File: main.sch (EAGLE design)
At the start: 7 parts

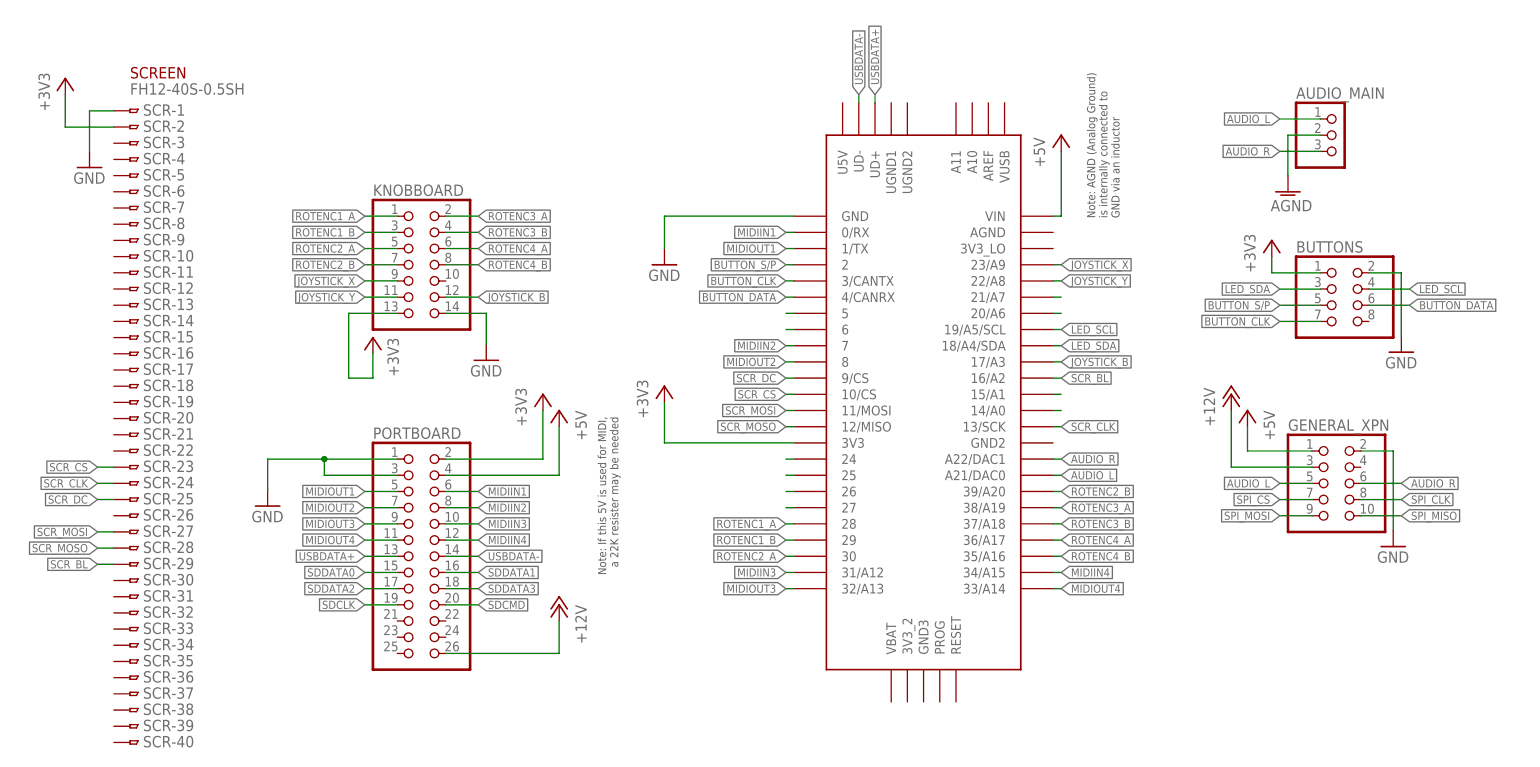
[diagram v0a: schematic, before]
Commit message: xpn-SPI connected, portboard audio added
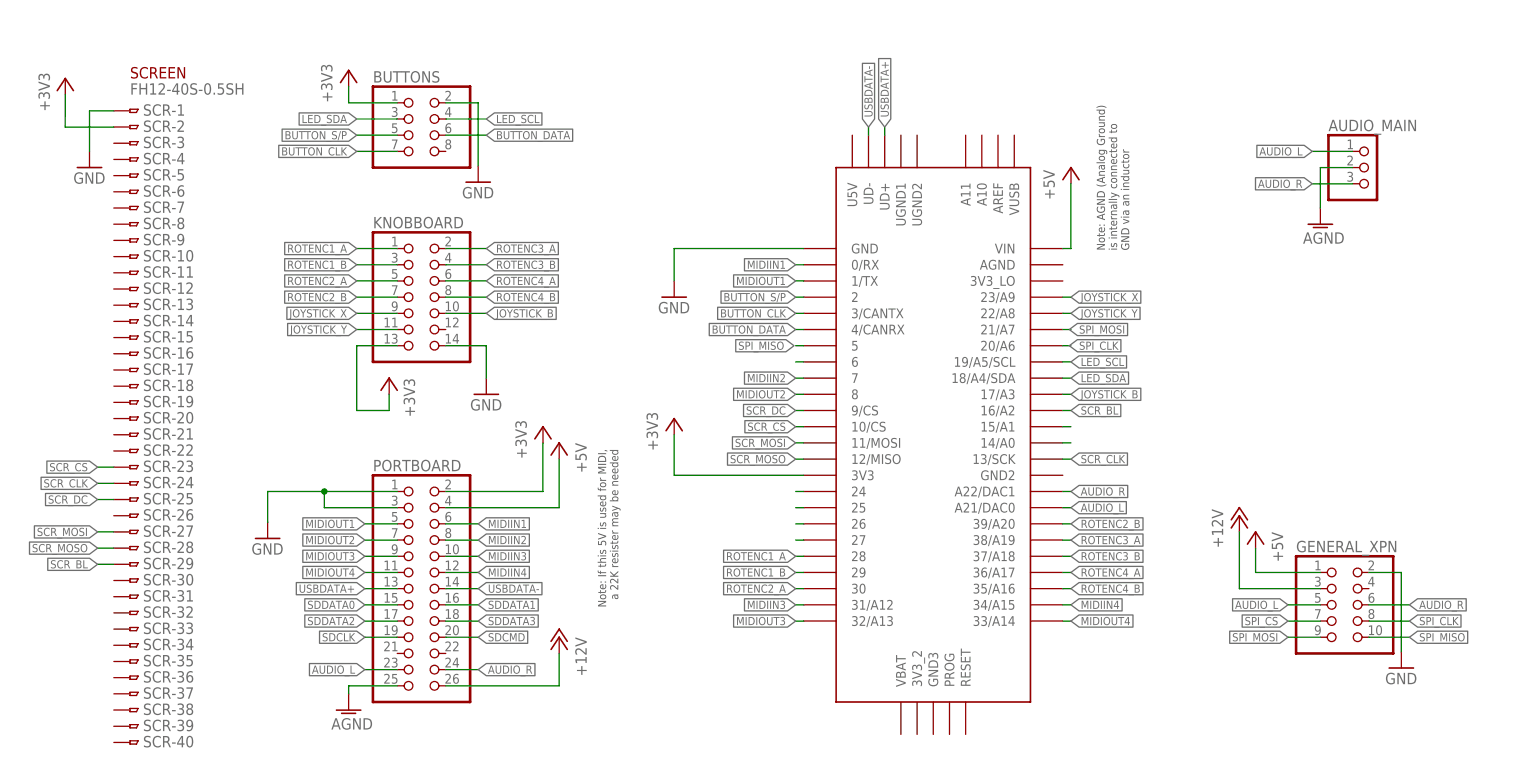
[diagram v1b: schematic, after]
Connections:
- removed net N$1: U$1.5
- removed net N$20: U$1.21/A7
- removed net N$21: U$1.20/A6
- net AGND: now also PORTBOARD.25
- net AUDIO_L: now also PORTBOARD.23
- net AUDIO_R: now also PORTBOARD.24
- net JOYSTICK_B: now also KNOBBOARD.10; no longer KNOBBOARD.12
- net SPI_CLK: now also U$1.20/A6
- net SPI_MISO: now also U$1.5
- net SPI_MOSI: now also U$1.21/A7
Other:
- moved on the sheet: AUDIO_MAIN, BUTTONS, GENERAL_XPN, KNOBBOARD, PORTBOARD

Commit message: milestone, reroute
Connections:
- net AUDIO_L: now also GENERAL_XPN.7; no longer GENERAL_XPN.5
- net AUDIO_R: now also GENERAL_XPN.9; no longer GENERAL_XPN.6
- net GND: now also GENERAL_XPN.5; no longer GENERAL_XPN.2
- net SPI_CLK: now also GENERAL_XPN.2; no longer GENERAL_XPN.8
- net SPI_CS: now also GENERAL_XPN.8; no longer GENERAL_XPN.7
- net SPI_MISO: now also GENERAL_XPN.6; no longer GENERAL_XPN.10
- net SPI_MOSI: now also GENERAL_XPN.4; no longer GENERAL_XPN.9
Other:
- moved on the sheet: GENERAL_XPN
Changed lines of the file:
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@@
 <part name="GND5" library="supply1" library_urn="urn:adsk.eagle:library:371" deviceset="GND" device=""/>
 <part name="P+3" library="supply1" library_urn="urn:adsk.eagle:library:371" deviceset="+5V" device=""/>
-<part name="GND6" library="supply1" library_urn="urn:adsk.eagle:library:371" deviceset="GND" device=""/>
 <part name="P+4" library="supply1" library_urn="urn:adsk.eagle:library:371" deviceset="+12V" device=""/>
 <part name="P+5" library="supply1" library_urn="urn:adsk.eagle:library:371" deviceset="+12V" device=""/>
@@
 <part name="AGND1" library="supply1" library_urn="urn:adsk.eagle:library:371" deviceset="AGND" device=""/>
 <part name="AGND2" library="supply1" library_urn="urn:adsk.eagle:library:371" deviceset="AGND" device=""/>
+<part name="GND6" library="supply1" library_urn="urn:adsk.eagle:library:371" deviceset="GND" device=""/>
 </parts>
 <sheets>
@@
 <attribute name="VALUE" x="80.01" y="94.234" size="1.778" layer="96"/>
 </instance>
-<instance part="P+3" gate="1" x="204.47" y="41.91" smashed="yes">
-<attribute name="VALUE" x="207.01" y="41.91" size="1.778" layer="96" rot="R270"/>
-</instance>
-<instance part="GND6" gate="1" x="227.33" y="20.574" smashed="yes">
-<attribute name="VALUE" x="224.79" y="18.034" size="1.778" layer="96"/>
-</instance>
-<instance part="P+4" gate="1" x="201.93" y="44.45" smashed="yes">
-<attribute name="VALUE" x="199.39" y="39.37" size="1.778" layer="96" rot="R90"/>
+<instance part="P+3" gate="1" x="204.47" y="72.39" smashed="yes">
+<attribute name="VALUE" x="207.01" y="72.39" size="1.778" layer="96" rot="R270"/>
+</instance>
+<instance part="P+4" gate="1" x="201.93" y="74.93" smashed="yes">
+<attribute name="VALUE" x="199.39" y="69.85" size="1.778" layer="96" rot="R90"/>
 </instance>
 <instance part="P+5" gate="1" x="95.25" y="25.4" smashed="yes">
@@
 <attribute name="VALUE" x="66.04" y="96.52" size="1.778" layer="96"/>
 </instance>
-<instance part="GENERAL_XPN" gate="A" x="217.17" y="30.48" smashed="yes">
-<attribute name="NAME" x="210.82" y="38.735" size="1.778" layer="95"/>
-<attribute name="VALUE" x="210.82" y="20.32" size="1.778" layer="96"/>
+<instance part="GENERAL_XPN" gate="A" x="217.17" y="60.96" smashed="yes">
+<attribute name="NAME" x="210.82" y="69.215" size="1.778" layer="95"/>
+<attribute name="VALUE" x="210.82" y="50.8" size="1.778" layer="96"/>
 </instance>
 <instance part="AGND1" gate="VR1" x="214.63" y="90.17" smashed="yes">
@@
 <instance part="AGND2" gate="VR1" x="62.23" y="13.97" smashed="yes">
 <attribute name="VALUE" x="66.04" y="12.7" size="1.778" layer="96" rot="R180"/>
+</instance>
+<instance part="GND6" gate="1" x="196.85" y="50.8" smashed="yes">
+<attribute name="VALUE" x="194.31" y="48.26" size="1.778" layer="96"/>
 </instance>
 </instances>
@@
 <wire x1="82.55" y1="109.22" x2="82.55" y2="99.314" width="0.1524" layer="91"/>
 <pinref part="BUTTONS" gate="A" pin="2"/>
-</segment>
-<segment>
-<wire x1="222.25" y1="35.56" x2="227.33" y2="35.56" width="0.1524" layer="91"/>
-<pinref part="GND6" gate="1" pin="GND"/>
-<wire x1="227.33" y1="23.114" x2="227.33" y2="35.56" width="0.1524" layer="91"/>
-<pinref part="GENERAL_XPN" gate="A" pin="2"/>
 </segment>
 <segment>
@@
 <pinref part="PORTBOARD" gate="A" pin="3"/>
 </segment>
+<segment>
+<wire x1="214.63" y1="60.96" x2="196.85" y2="60.96" width="0.1524" layer="91"/>
+<wire x1="196.85" y1="60.96" x2="196.85" y2="53.34" width="0.1524" layer="91"/>
+<pinref part="GENERAL_XPN" gate="A" pin="5"/>
+<pinref part="GND6" gate="1" pin="GND"/>
+</segment>
 </net>
 <net name="+3V3" class="0">
@@
 </segment>
 <segment>
-<wire x1="214.63" y1="35.56" x2="204.47" y2="35.56" width="0.1524" layer="91"/>
+<wire x1="214.63" y1="66.04" x2="204.47" y2="66.04" width="0.1524" layer="91"/>
 <pinref part="P+3" gate="1" pin="+5V"/>
-<wire x1="204.47" y1="35.56" x2="204.47" y2="39.37" width="0.1524" layer="91"/>
+<wire x1="204.47" y1="66.04" x2="204.47" y2="69.85" width="0.1524" layer="91"/>
 <pinref part="GENERAL_XPN" gate="A" pin="1"/>
 </segment>
@@
 </segment>
 <segment>
-<wire x1="222.25" y1="30.48" x2="228.6" y2="30.48" width="0.1524" layer="91"/>
-<label x="228.6" y="30.48" size="1.27" layer="95" xref="yes"/>
-<pinref part="GENERAL_XPN" gate="A" pin="6"/>
-</segment>
-<segment>
 <pinref part="PORTBOARD" gate="A" pin="24"/>
 <wire x1="77.47" y1="20.32" x2="82.55" y2="20.32" width="0.1524" layer="91"/>
 <label x="82.55" y="20.32" size="1.27" layer="95" xref="yes"/>
 </segment>
+<segment>
+<pinref part="GENERAL_XPN" gate="A" pin="9"/>
+<wire x1="214.63" y1="55.88" x2="208.28" y2="55.88" width="0.1524" layer="91"/>
+<label x="208.28" y="55.88" size="1.27" layer="95" rot="R180" xref="yes"/>
+</segment>
 </net>
 <net name="AUDIO_L" class="0">
@@
 </segment>
 <segment>
-<wire x1="214.63" y1="30.48" x2="209.55" y2="30.48" width="0.1524" layer="91"/>
-<label x="209.55" y="30.48" size="1.27" layer="95" rot="R180" xref="yes"/>
-<pinref part="GENERAL_XPN" gate="A" pin="5"/>
-</segment>
-<segment>
 <pinref part="PORTBOARD" gate="A" pin="23"/>
 <wire x1="69.85" y1="20.32" x2="64.77" y2="20.32" width="0.1524" layer="91"/>
 <label x="64.77" y="20.32" size="1.27" layer="95" rot="R180" xref="yes"/>
 </segment>
+<segment>
+<pinref part="GENERAL_XPN" gate="A" pin="7"/>
+<wire x1="214.63" y1="58.42" x2="208.28" y2="58.42" width="0.1524" layer="91"/>
+<label x="208.28" y="58.42" size="1.27" layer="95" rot="R180" xref="yes"/>
+</segment>
 </net>
 <net name="MIDIOUT1" class="0">
@@
 </segment>
 </net>
-<net name="SPI_CS" class="0">
-<segment>
-<wire x1="214.63" y1="27.94" x2="209.55" y2="27.94" width="0.1524" layer="91"/>
-<label x="209.55" y="27.94" size="1.27" layer="95" rot="R180" xref="yes"/>
-<pinref part="GENERAL_XPN" gate="A" pin="7"/>
-</segment>
-</net>
 <net name="SPI_CLK" class="0">
-<segment>
-<wire x1="222.25" y1="27.94" x2="228.6" y2="27.94" width="0.1524" layer="91"/>
-<label x="228.6" y="27.94" size="1.27" layer="95" xref="yes"/>
-<pinref part="GENERAL_XPN" gate="A" pin="8"/>
-</segment>
 <segment>
 <pinref part="U$1" gate="G$1" pin="20/A6"/>
@@
 <label x="175.26" y="71.12" size="1.27" layer="95" xref="yes"/>
 </segment>
+<segment>
+<pinref part="GENERAL_XPN" gate="A" pin="2"/>
+<wire x1="222.25" y1="66.04" x2="228.6" y2="66.04" width="0.1524" layer="91"/>
+<label x="228.6" y="66.04" size="1.27" layer="95" xref="yes"/>
+</segment>
 </net>
 <net name="SPI_MOSI" class="0">
-<segment>
-<wire x1="214.63" y1="25.4" x2="209.55" y2="25.4" width="0.1524" layer="91"/>
-<label x="209.55" y="25.4" size="1.27" layer="95" rot="R180" xref="yes"/>
-<pinref part="GENERAL_XPN" gate="A" pin="9"/>
-</segment>
 <segment>
 <pinref part="U$1" gate="G$1" pin="21/A7"/>
@@
 <label x="175.26" y="73.66" size="1.27" layer="95" xref="yes"/>
 </segment>
+<segment>
+<pinref part="GENERAL_XPN" gate="A" pin="4"/>
+<wire x1="222.25" y1="63.5" x2="228.6" y2="63.5" width="0.1524" layer="91"/>
+<label x="228.6" y="63.5" size="1.27" layer="95" xref="yes"/>
+</segment>
 </net>
 <net name="SPI_MISO" class="0">
-<segment>
-<wire x1="222.25" y1="25.4" x2="228.6" y2="25.4" width="0.1524" layer="91"/>
-<label x="228.6" y="25.4" size="1.27" layer="95" xref="yes"/>
-<pinref part="GENERAL_XPN" gate="A" pin="10"/>
-</segment>
 <segment>
 <pinref part="U$1" gate="G$1" pin="5"/>
@@
 <label x="132.08" y="71.12" size="1.27" layer="95" rot="R180" xref="yes"/>
 </segment>
+<segment>
+<pinref part="GENERAL_XPN" gate="A" pin="6"/>
+<wire x1="222.25" y1="60.96" x2="228.6" y2="60.96" width="0.1524" layer="91"/>
+<label x="228.6" y="60.96" size="1.27" layer="95" xref="yes"/>
+</segment>
 </net>
 <net name="+12V" class="0">
 <segment>
 <pinref part="P+4" gate="1" pin="+12V"/>
-<wire x1="214.63" y1="33.02" x2="201.93" y2="33.02" width="0.1524" layer="91"/>
-<wire x1="201.93" y1="33.02" x2="201.93" y2="41.91" width="0.1524" layer="91"/>
+<wire x1="214.63" y1="63.5" x2="201.93" y2="63.5" width="0.1524" layer="91"/>
+<wire x1="201.93" y1="63.5" x2="201.93" y2="72.39" width="0.1524" layer="91"/>
 <pinref part="GENERAL_XPN" gate="A" pin="3"/>
 </segment>
@@
 </segment>
 </net>
+<net name="SPI_CS" class="0">
+<segment>
+<pinref part="GENERAL_XPN" gate="A" pin="8"/>
+<wire x1="222.25" y1="58.42" x2="228.6" y2="58.42" width="0.1524" layer="91"/>
+<label x="228.6" y="58.42" size="1.27" layer="95" xref="yes"/>
+</segment>
+</net>

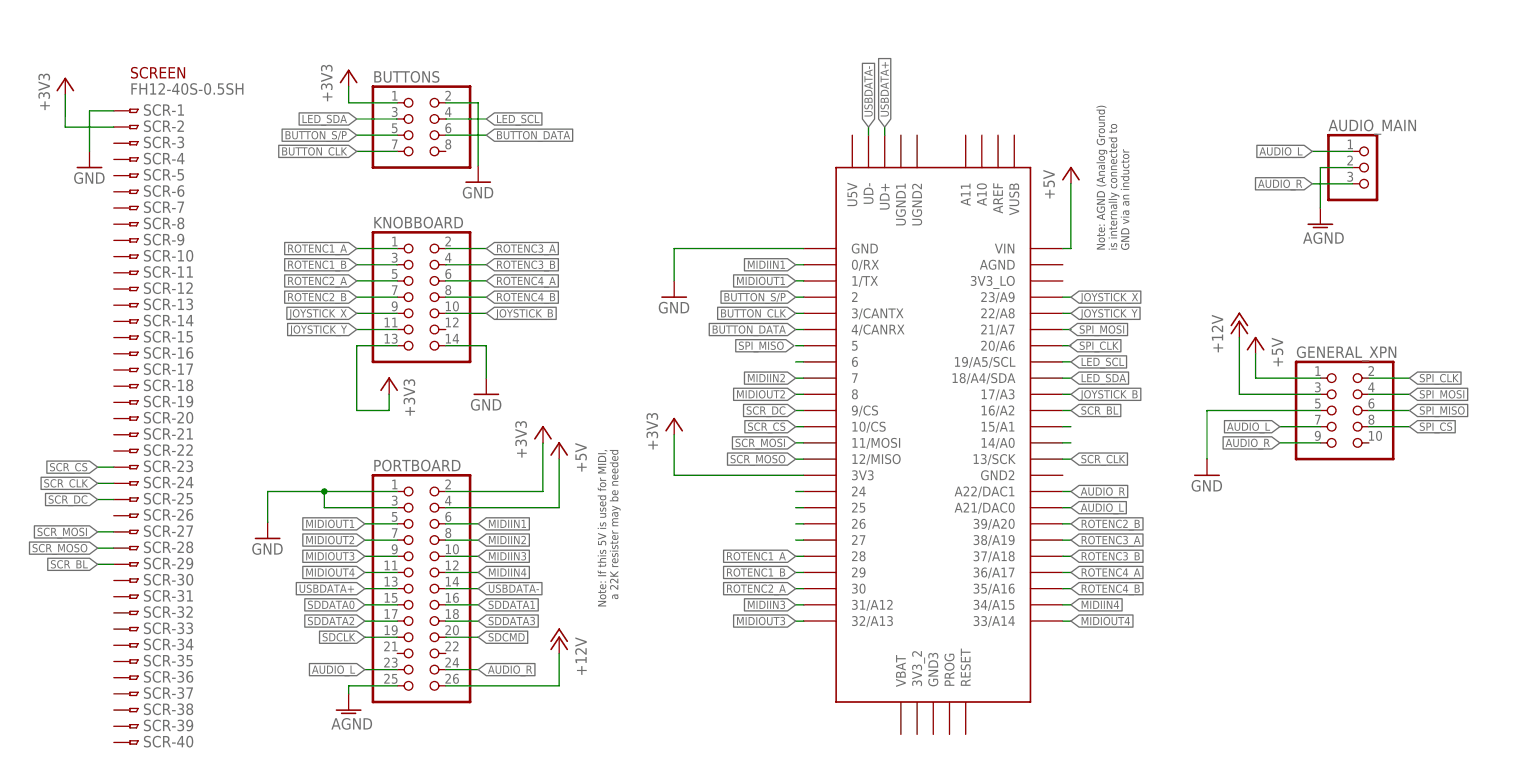
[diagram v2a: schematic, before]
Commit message: Added 8 channel audio xpn to general board (inc. pdf)
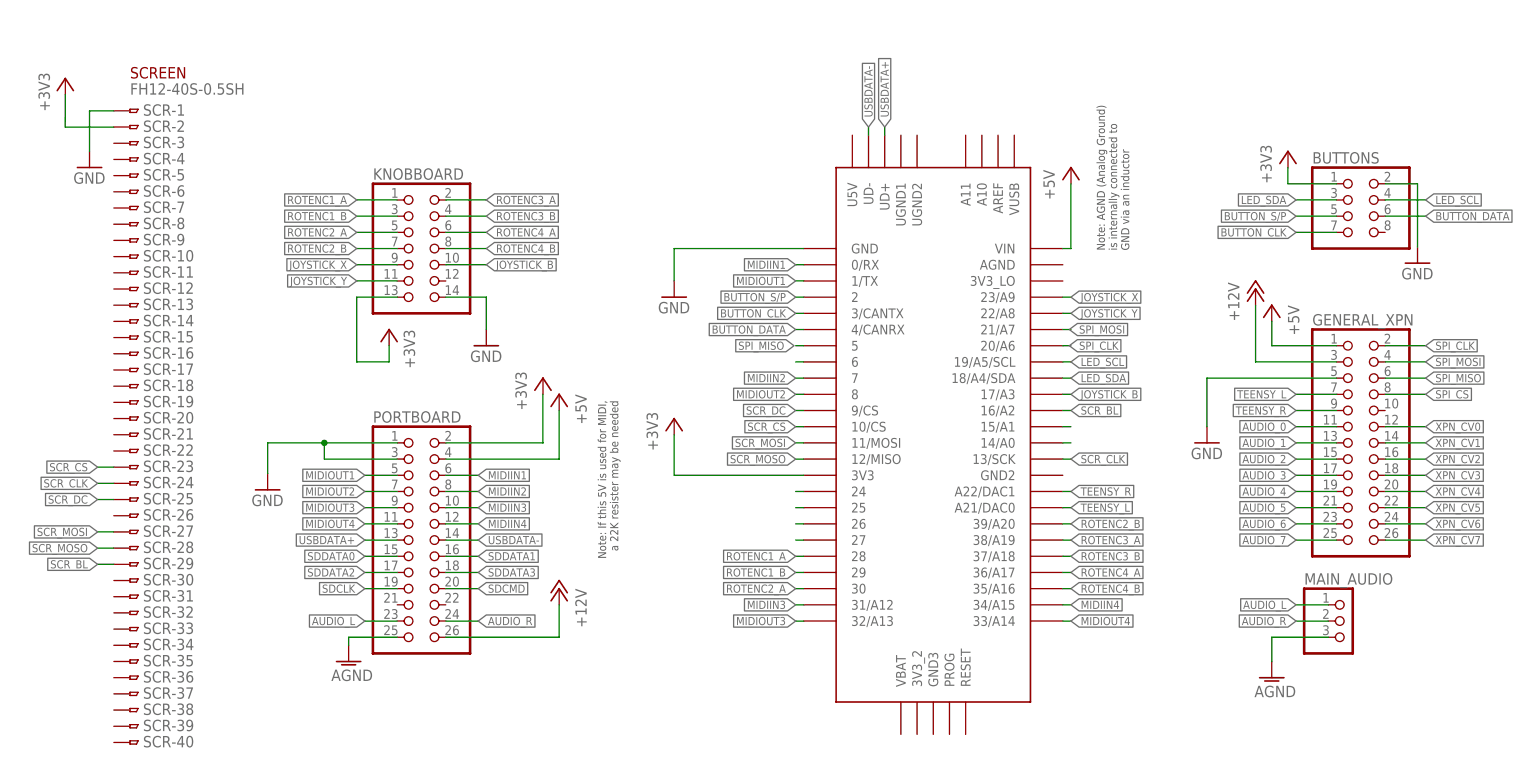
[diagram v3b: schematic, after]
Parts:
- removed AUDIO_MAIN: (no value), pinhead:PINHD-1X3
- added MAIN_AUDIO: (no value), pinhead:PINHD-1X3
- GENERAL_XPN: device pinhead:PINHD-2X5 -> pinhead:PINHD-2X13
- renumbered U$1 to TEENSY_3.6
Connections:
- new net AUDIO_0: GENERAL_XPN.11
- new net AUDIO_1: GENERAL_XPN.13
- new net AUDIO_2: GENERAL_XPN.15
- new net AUDIO_3: GENERAL_XPN.17
- new net AUDIO_4: GENERAL_XPN.19
- new net AUDIO_5: GENERAL_XPN.21
- new net AUDIO_6: GENERAL_XPN.23
- new net AUDIO_7: GENERAL_XPN.25
- new net TEENSY_L: GENERAL_XPN.7, TEENSY_3.6.A21/DAC0
- new net TEENSY_R: GENERAL_XPN.9, TEENSY_3.6.A22/DAC1
- new net XPN_CV0: GENERAL_XPN.12
- new net XPN_CV1: GENERAL_XPN.14
- new net XPN_CV2: GENERAL_XPN.16
- new net XPN_CV3: GENERAL_XPN.18
- new net XPN_CV4: GENERAL_XPN.20
- new net XPN_CV5: GENERAL_XPN.22
- new net XPN_CV6: GENERAL_XPN.24
- new net XPN_CV7: GENERAL_XPN.26
- net AGND: now also MAIN_AUDIO.3; no longer AUDIO_MAIN.2
- net AUDIO_L: now also MAIN_AUDIO.1; no longer AUDIO_MAIN.1, GENERAL_XPN.7, TEENSY_3.6.A21/DAC0
- net AUDIO_R: now also MAIN_AUDIO.2; no longer AUDIO_MAIN.3, GENERAL_XPN.9, TEENSY_3.6.A22/DAC1
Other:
- moved on the sheet: BUTTONS, KNOBBOARD, PORTBOARD
